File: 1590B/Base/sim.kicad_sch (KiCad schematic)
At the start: 14 parts

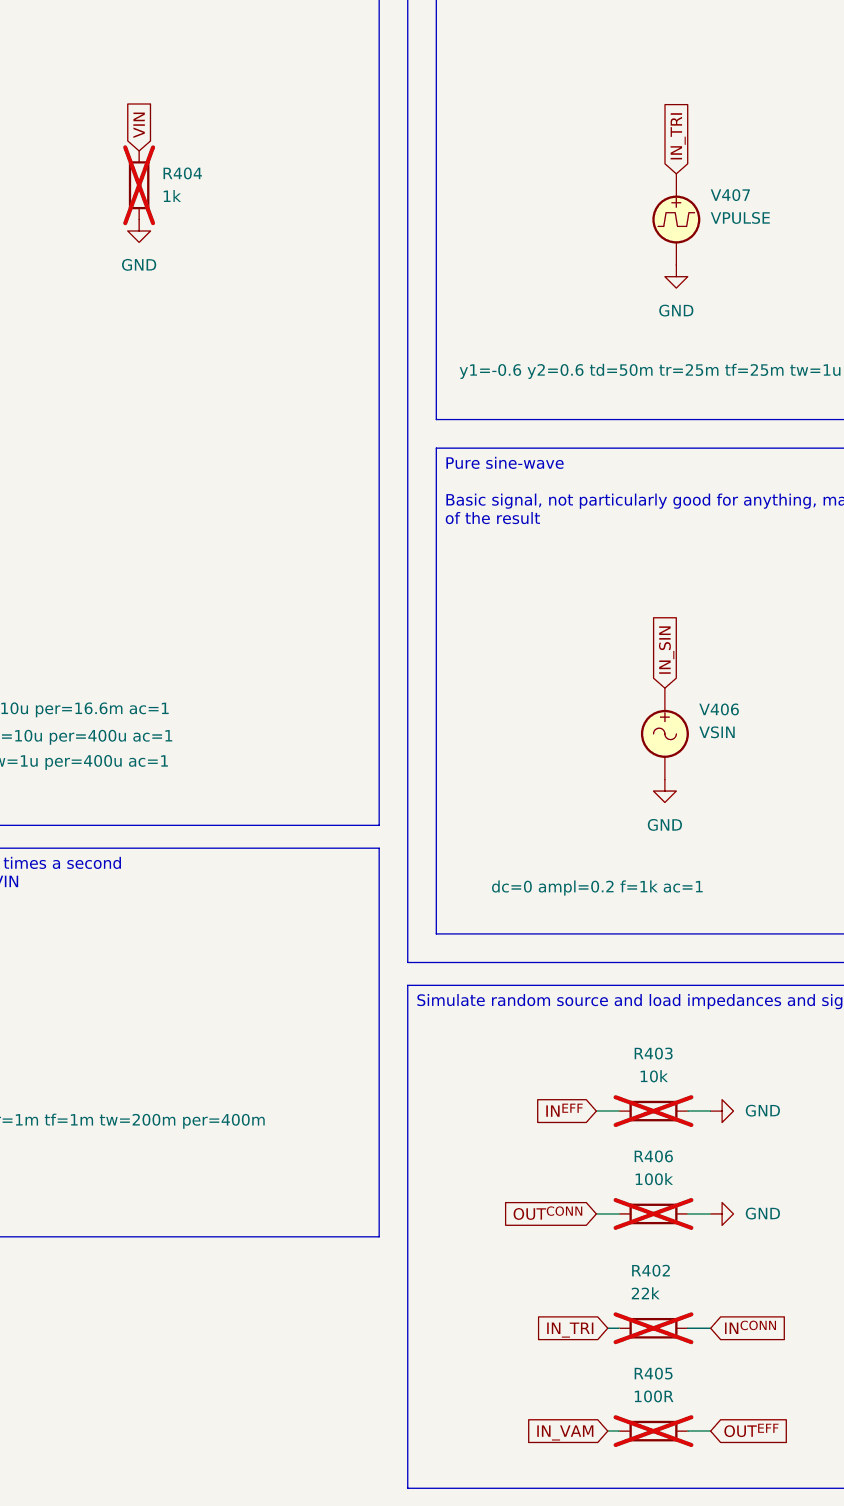
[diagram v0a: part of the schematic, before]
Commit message: Update 1590B board for sanity
I had entirely forgotten the activity LED, which was really annoying
when testing.

Also, while the transistor follower / capacitor multiplier on the analog
power supply was interesting for some low frequency power supply ripple
removal in simulation, it doesn't actually make any sense with any
modern power supply, so just do a regular RC filter for high
frequencies, which is what actually matters.

Together with the fixed potentiometer board, I think this should now
work nicely.

Famous last words.

Signed-off-by: Linus Torvalds <torvalds@linux-foundation.org>
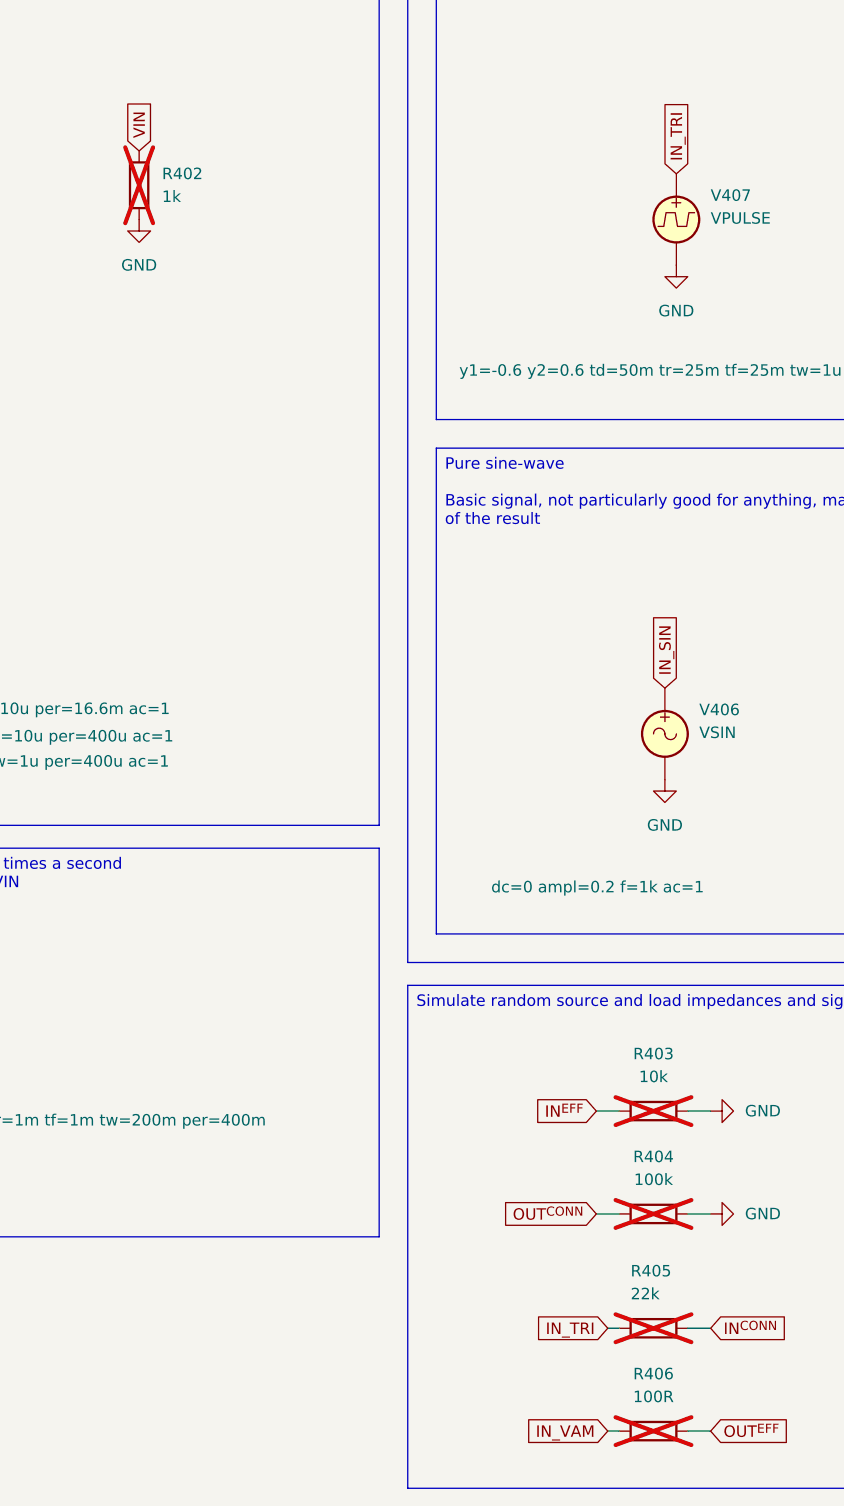
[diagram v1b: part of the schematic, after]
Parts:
- renumbered R404 to R402, R406 to R404, R402 to R405, R405 to R406
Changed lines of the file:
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@@
 		(on_board no)
 		(dnp yes)
-		(property "Reference" "R405"
+		(property "Reference" "R406"
 			(at 125.73 179.07 90)
 			(effects
@@
 			(project "Jacks"
 				(path "/9e337e0b-885b-4d2b-99a2-62cdd082c615/a1084b87-85fd-4b63-8fe4-8749c999d338"
-					(reference "R405")
+					(reference "R406")
 					(unit 1)
 				)
@@
 		(dnp yes)
 		(fields_autoplaced yes)
-		(property "Reference" "R406"
+		(property "Reference" "R404"
 			(at 125.73 154.94 90)
 			(effects
@@
 			(project "Jacks"
 				(path "/9e337e0b-885b-4d2b-99a2-62cdd082c615/a1084b87-85fd-4b63-8fe4-8749c999d338"
-					(reference "R406")
+					(reference "R404")
 					(unit 1)
 				)
@@
 		(on_board no)
 		(dnp yes)
-		(property "Reference" "R402"
+		(property "Reference" "R405"
 			(at 123.19 167.6399 90)
 			(effects
@@
 			(project "Buffered"
 				(path "/9e337e0b-885b-4d2b-99a2-62cdd082c615/a1084b87-85fd-4b63-8fe4-8749c999d338"
-					(reference "R402")
+					(reference "R405")
 					(unit 1)
 				)
@@
 		(dnp yes)
 		(fields_autoplaced yes)
-		(property "Reference" "R404"
+		(property "Reference" "R402"
 			(at 71.12 45.7199 0)
 			(effects
@@
 			(project "Buffered"
 				(path "/9e337e0b-885b-4d2b-99a2-62cdd082c615/a1084b87-85fd-4b63-8fe4-8749c999d338"
-					(reference "R404")
-					(unit 1)
-				)
+					(reference "R402")
+					(unit 1)
+				)
